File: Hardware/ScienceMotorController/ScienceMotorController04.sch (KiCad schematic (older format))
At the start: 4 parts

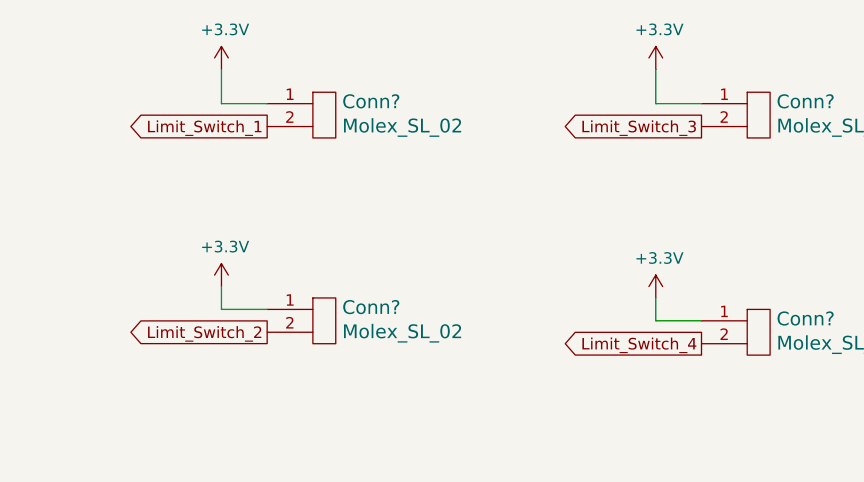
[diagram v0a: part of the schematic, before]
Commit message: limit switch indicators
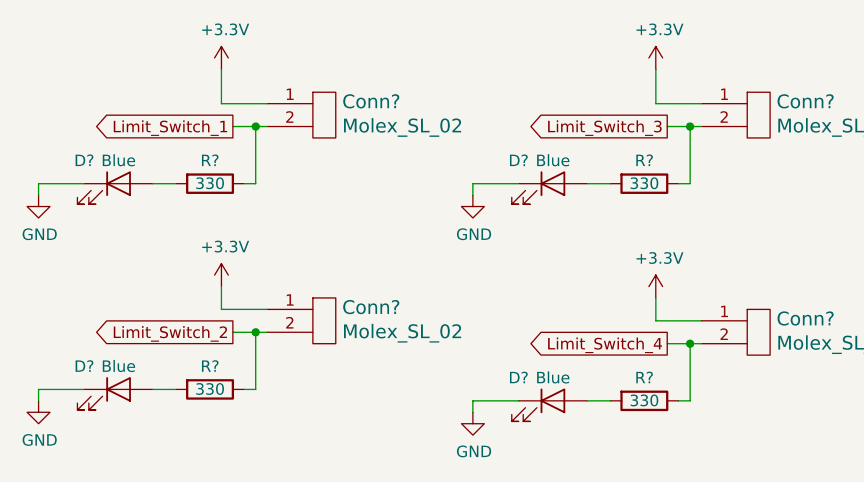
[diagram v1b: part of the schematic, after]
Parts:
- added D? (x4): Blue, symbol Device:LED
- added R? (x4): 330, symbol Device:R
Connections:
- net Limit_Switch_1: now also R?.1
- net Limit_Switch_2: now also R?.1
- net Limit_Switch_3: now also R?.1
- net Limit_Switch_4: now also R?.1
- new net: D?.2 (A), R?.2 (x4)
- new net GND: D?.1 (K), D?.1 (K), D?.1 (K), D?.1 (K)
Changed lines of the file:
@@
 $Descr A4 11693 8268
 encoding utf-8
-Sheet 5 11
+Sheet 11 11
 Title ""
 Date ""
@@
 Wire Wire Line
 	4150 2950 4350 2950
-Text GLabel 2450 2100 0    50   Output ~ 0
+Text GLabel 2300 2100 0    50   Output ~ 0
 Limit_Switch_1
-Text GLabel 2450 3000 0    50   Output ~ 0
+Text GLabel 2300 3000 0    50   Output ~ 0
 Limit_Switch_2
-Text GLabel 4350 2100 0    50   Output ~ 0
+Text GLabel 4200 2100 0    50   Output ~ 0
 Limit_Switch_3
-Text GLabel 4350 3050 0    50   Output ~ 0
+Text GLabel 4200 3050 0    50   Output ~ 0
 Limit_Switch_4
+Wire Wire Line
+	4350 2100 4300 2100
+Wire Wire Line
+	2450 2100 2400 2100
+Wire Wire Line
+	2450 3000 2400 3000
+Wire Wire Line
+	4200 3050 4300 3050
+$Comp
+L Device:LED D?
+U 1 1 5FAEAF9B
+P 3700 2350
+F 0 "D?" H 3550 2450 50  0000 C CNN
+F 1 "Blue" H 3700 2450 50  0000 C CNN
+F 2 "" H 3700 2350 50  0001 C CNN
+F 3 "~" H 3700 2350 50  0001 C CNN
+	1    3700 2350
+	1    0    0    -1
+$EndComp
+$Comp
+L Device:LED D?
+U 1 1 5FAEC8F1
+P 1800 2350
+F 0 "D?" H 1650 2450 50  0000 C CNN
+F 1 "Blue" H 1800 2450 50  0000 C CNN
+F 2 "" H 1800 2350 50  0001 C CNN
+F 3 "~" H 1800 2350 50  0001 C CNN
+	1    1800 2350
+	1    0    0    -1
+$EndComp
+$Comp
+L Device:LED D?
+U 1 1 5FAEE0DE
+P 1800 3250
+F 0 "D?" H 1650 3350 50  0000 C CNN
+F 1 "Blue" H 1800 3350 50  0000 C CNN
+F 2 "" H 1800 3250 50  0001 C CNN
+F 3 "~" H 1800 3250 50  0001 C CNN
+	1    1800 3250
+	1    0    0    -1
+$EndComp
+$Comp
+L Device:LED D?
+U 1 1 5FAEEC9D
+P 3700 3300
+F 0 "D?" H 3550 3400 50  0000 C CNN
+F 1 "Blue" H 3700 3400 50  0000 C CNN
+F 2 "" H 3700 3300 50  0001 C CNN
+F 3 "~" H 3700 3300 50  0001 C CNN
+	1    3700 3300
+	1    0    0    -1
+$EndComp
+$Comp
+L Device:R R?
+U 1 1 5FAEFC97
+P 4100 2350
+F 0 "R?" V 4000 2350 50  0000 C CNN
+F 1 "330" V 4100 2350 50  0000 C CNN
+F 2 "" V 4030 2350 50  0001 C CNN
+F 3 "~" H 4100 2350 50  0001 C CNN
+	1    4100 2350
+	0    1    1    0
+$EndComp
+Wire Wire Line
+	4250 2350 4300 2350
+Wire Wire Line
+	4300 2350 4300 2100
+Connection ~ 4300 2100
+Wire Wire Line
+	4300 2100 4200 2100
+Wire Wire Line
+	3950 2350 3850 2350
+$Comp
+L Device:R R?
+U 1 1 5FAF1AC8
+P 2200 2350
+F 0 "R?" V 2100 2350 50  0000 C CNN
+F 1 "330" V 2200 2350 50  0000 C CNN
+F 2 "" V 2130 2350 50  0001 C CNN
+F 3 "~" H 2200 2350 50  0001 C CNN
+	1    2200 2350
+	0    1    1    0
+$EndComp
+Wire Wire Line
+	2400 2100 2400 2350
+Wire Wire Line
+	2400 2350 2350 2350
+Connection ~ 2400 2100
+Wire Wire Line
+	2400 2100 2300 2100
+Wire Wire Line
+	1950 2350 2050 2350
+$Comp
+L Device:R R?
+U 1 1 5FAF47E1
+P 4100 3300
+F 0 "R?" V 4000 3300 50  0000 C CNN
+F 1 "330" V 4100 3300 50  0000 C CNN
+F 2 "" V 4030 3300 50  0001 C CNN
+F 3 "~" H 4100 3300 50  0001 C CNN
+	1    4100 3300
+	0    1    1    0
+$EndComp
+Wire Wire Line
+	3850 3300 3950 3300
+Wire Wire Line
+	4250 3300 4300 3300
+Wire Wire Line
+	4300 3300 4300 3050
+Connection ~ 4300 3050
+Wire Wire Line
+	4300 3050 4350 3050
+$Comp
+L Device:R R?
+U 1 1 5FAF884A
+P 2200 3250
+F 0 "R?" V 2100 3250 50  0000 C CNN
+F 1 "330" V 2200 3250 50  0000 C CNN
+F 2 "" V 2130 3250 50  0001 C CNN
+F 3 "~" H 2200 3250 50  0001 C CNN
+	1    2200 3250
+	0    1    1    0
+$EndComp
+Wire Wire Line
+	1950 3250 2050 3250
+Wire Wire Line
+	2350 3250 2400 3250
+Wire Wire Line
+	2400 3250 2400 3000
+Connection ~ 2400 3000
+Wire Wire Line
+	2400 3000 2300 3000
+$Comp
+L power:GND #PWR?
+U 1 1 5FAFA721
+P 3350 2400
+F 0 "#PWR?" H 3350 2150 50  0001 C CNN
+F 1 "GND" H 3355 2227 50  0000 C CNN
+F 2 "" H 3350 2400 50  0001 C CNN
+F 3 "" H 3350 2400 50  0001 C CNN
+	1    3350 2400
+	1    0    0    -1
+$EndComp
+$Comp
+L power:GND #PWR?
+U 1 1 5FAFC4B8
+P 1450 2400
+F 0 "#PWR?" H 1450 2150 50  0001 C CNN
+F 1 "GND" H 1455 2227 50  0000 C CNN
+F 2 "" H 1450 2400 50  0001 C CNN
+F 3 "" H 1450 2400 50  0001 C CNN
+	1    1450 2400
+	1    0    0    -1
+$EndComp
+$Comp
+L power:GND #PWR?
+U 1 1 5FAFD70B
+P 1450 3300
+F 0 "#PWR?" H 1450 3050 50  0001 C CNN
+F 1 "GND" H 1455 3127 50  0000 C CNN
+F 2 "" H 1450 3300 50  0001 C CNN
+F 3 "" H 1450 3300 50  0001 C CNN
+	1    1450 3300
+	1    0    0    -1
+$EndComp
+$Comp
+L power:GND #PWR?
+U 1 1 5FAFEF1A
+P 3350 3350
+F 0 "#PWR?" H 3350 3100 50  0001 C CNN
+F 1 "GND" H 3355 3177 50  0000 C CNN
+F 2 "" H 3350 3350 50  0001 C CNN
+F 3 "" H 3350 3350 50  0001 C CNN
+	1    3350 3350
+	1    0    0    -1
+$EndComp
+Wire Wire Line
+	3550 2350 3350 2350
+Wire Wire Line
+	3350 2350 3350 2400
+Wire Wire Line
+	3350 3350 3350 3300
+Wire Wire Line
+	3350 3300 3550 3300
+Wire Wire Line
+	1650 2350 1450 2350
+Wire Wire Line
+	1450 2350 1450 2400
+Wire Wire Line
+	1450 3300 1450 3250
+Wire Wire Line
+	1450 3250 1650 3250
 $EndSCHEMATC

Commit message: made some more hierarchal changes
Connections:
- net +3V3 renamed 3.3VA
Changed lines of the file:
@@
 $Descr A4 11693 8268
 encoding utf-8
-Sheet 11 10
+Sheet 4 10
 Title ""
 Date ""
@@
 	1    0    0    -1
 $EndComp
-$Comp
-L power:+3.3V #PWR?
-U 1 1 5F81D779
-P 2250 1850
-F 0 "#PWR?" H 2250 1700 50  0001 C CNN
-F 1 "+3.3V" H 2265 2023 50  0000 C CNN
-F 2 "" H 2250 1850 50  0001 C CNN
-F 3 "" H 2250 1850 50  0001 C CNN
-	1    2250 1850
-	1    0    0    -1
-$EndComp
-$Comp
-L power:+3.3V #PWR?
-U 1 1 5F81DF85
-P 4150 1850
-F 0 "#PWR?" H 4150 1700 50  0001 C CNN
-F 1 "+3.3V" H 4165 2023 50  0000 C CNN
-F 2 "" H 4150 1850 50  0001 C CNN
-F 3 "" H 4150 1850 50  0001 C CNN
-	1    4150 1850
-	1    0    0    -1
-$EndComp
-$Comp
-L power:+3.3V #PWR?
-U 1 1 5F81E7D7
-P 2250 2800
-F 0 "#PWR?" H 2250 2650 50  0001 C CNN
-F 1 "+3.3V" H 2265 2973 50  0000 C CNN
-F 2 "" H 2250 2800 50  0001 C CNN
-F 3 "" H 2250 2800 50  0001 C CNN
-	1    2250 2800
-	1    0    0    -1
-$EndComp
-$Comp
-L power:+3.3V #PWR?
-U 1 1 5F81F2A0
-P 4150 2850
-F 0 "#PWR?" H 4150 2700 50  0001 C CNN
-F 1 "+3.3V" H 4165 3023 50  0000 C CNN
-F 2 "" H 4150 2850 50  0001 C CNN
-F 3 "" H 4150 2850 50  0001 C CNN
-	1    4150 2850
-	1    0    0    -1
-$EndComp
 Wire Wire Line
 	2250 1850 2250 2000
@@
 Wire Wire Line
 	1450 3250 1650 3250
+Text HLabel 2250 1850 1    50   Input ~ 0
+3.3VA
+Text HLabel 4150 1850 1    50   Input ~ 0
+3.3VA
+Text HLabel 2250 2800 1    50   Input ~ 0
+3.3VA
+Text HLabel 4150 2850 1    50   Input ~ 0
+3.3VA
 $EndSCHEMATC

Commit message: fixed hierarchical
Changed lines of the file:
@@
 $Descr A4 11693 8268
 encoding utf-8
-Sheet 4 10
+Sheet 9 11
 Title ""
 Date ""
@@
 U 1 1 5F81B312
 P 2650 2150
+AR Path="/5F81B171/5F81B312" Ref="Conn?"  Part="1"
+AR Path="/5F7148FA/5FC42AEE/5F81B312" Ref="Conn?"  Part="1"
 F 0 "Conn?" H 2778 2308 60  0000 L CNN
 F 1 "Molex_SL_02" H 2778 2202 60  0000 L CNN
@@
 U 1 1 5F81C1D4
 P 4550 2150
+AR Path="/5F81B171/5F81C1D4" Ref="Conn?"  Part="1"
+AR Path="/5F7148FA/5FC42AEE/5F81C1D4" Ref="Conn?"  Part="1"
 F 0 "Conn?" H 4678 2308 60  0000 L CNN
 F 1 "Molex_SL_02" H 4678 2202 60  0000 L CNN
@@
 U 1 1 5F81C7E8
 P 2650 3050
+AR Path="/5F81B171/5F81C7E8" Ref="Conn?"  Part="1"
+AR Path="/5F7148FA/5FC42AEE/5F81C7E8" Ref="Conn?"  Part="1"
 F 0 "Conn?" H 2778 3208 60  0000 L CNN
 F 1 "Molex_SL_02" H 2778 3102 60  0000 L CNN
@@
 U 1 1 5F81D13D
 P 4550 3100
+AR Path="/5F81B171/5F81D13D" Ref="Conn?"  Part="1"
+AR Path="/5F7148FA/5FC42AEE/5F81D13D" Ref="Conn?"  Part="1"
 F 0 "Conn?" H 4678 3258 60  0000 L CNN
 F 1 "Molex_SL_02" H 4678 3152 60  0000 L CNN
@@
 Wire Wire Line
 	4150 2950 4350 2950
-Text GLabel 2300 2100 0    50   Output ~ 0
-Limit_Switch_1
-Text GLabel 2300 3000 0    50   Output ~ 0
-Limit_Switch_2
-Text GLabel 4200 2100 0    50   Output ~ 0
-Limit_Switch_3
-Text GLabel 4200 3050 0    50   Output ~ 0
-Limit_Switch_4
 Wire Wire Line
 	4350 2100 4300 2100
@@
 U 1 1 5FAEAF9B
 P 3700 2350
+AR Path="/5F81B171/5FAEAF9B" Ref="D?"  Part="1"
+AR Path="/5F7148FA/5FC42AEE/5FAEAF9B" Ref="D?"  Part="1"
 F 0 "D?" H 3550 2450 50  0000 C CNN
 F 1 "Blue" H 3700 2450 50  0000 C CNN
@@
 U 1 1 5FAEC8F1
 P 1800 2350
+AR Path="/5F81B171/5FAEC8F1" Ref="D?"  Part="1"
+AR Path="/5F7148FA/5FC42AEE/5FAEC8F1" Ref="D?"  Part="1"
 F 0 "D?" H 1650 2450 50  0000 C CNN
 F 1 "Blue" H 1800 2450 50  0000 C CNN
@@
 U 1 1 5FAEE0DE
 P 1800 3250
+AR Path="/5F81B171/5FAEE0DE" Ref="D?"  Part="1"
+AR Path="/5F7148FA/5FC42AEE/5FAEE0DE" Ref="D?"  Part="1"
 F 0 "D?" H 1650 3350 50  0000 C CNN
 F 1 "Blue" H 1800 3350 50  0000 C CNN
@@
 U 1 1 5FAEEC9D
 P 3700 3300
+AR Path="/5F81B171/5FAEEC9D" Ref="D?"  Part="1"
+AR Path="/5F7148FA/5FC42AEE/5FAEEC9D" Ref="D?"  Part="1"
 F 0 "D?" H 3550 3400 50  0000 C CNN
 F 1 "Blue" H 3700 3400 50  0000 C CNN
@@
 U 1 1 5FAEFC97
 P 4100 2350
+AR Path="/5F81B171/5FAEFC97" Ref="R?"  Part="1"
+AR Path="/5F7148FA/5FC42AEE/5FAEFC97" Ref="R?"  Part="1"
 F 0 "R?" V 4000 2350 50  0000 C CNN
 F 1 "330" V 4100 2350 50  0000 C CNN
@@
 U 1 1 5FAF1AC8
 P 2200 2350
+AR Path="/5F81B171/5FAF1AC8" Ref="R?"  Part="1"
+AR Path="/5F7148FA/5FC42AEE/5FAF1AC8" Ref="R?"  Part="1"
 F 0 "R?" V 2100 2350 50  0000 C CNN
 F 1 "330" V 2200 2350 50  0000 C CNN
@@
 U 1 1 5FAF47E1
 P 4100 3300
+AR Path="/5F81B171/5FAF47E1" Ref="R?"  Part="1"
+AR Path="/5F7148FA/5FC42AEE/5FAF47E1" Ref="R?"  Part="1"
 F 0 "R?" V 4000 3300 50  0000 C CNN
 F 1 "330" V 4100 3300 50  0000 C CNN
@@
 U 1 1 5FAF884A
 P 2200 3250
+AR Path="/5F81B171/5FAF884A" Ref="R?"  Part="1"
+AR Path="/5F7148FA/5FC42AEE/5FAF884A" Ref="R?"  Part="1"
 F 0 "R?" V 2100 3250 50  0000 C CNN
 F 1 "330" V 2200 3250 50  0000 C CNN
@@
 U 1 1 5FAFA721
 P 3350 2400
+AR Path="/5F81B171/5FAFA721" Ref="#PWR?"  Part="1"
+AR Path="/5F7148FA/5FC42AEE/5FAFA721" Ref="#PWR?"  Part="1"
 F 0 "#PWR?" H 3350 2150 50  0001 C CNN
 F 1 "GND" H 3355 2227 50  0000 C CNN
@@
 U 1 1 5FAFC4B8
 P 1450 2400
+AR Path="/5F81B171/5FAFC4B8" Ref="#PWR?"  Part="1"
+AR Path="/5F7148FA/5FC42AEE/5FAFC4B8" Ref="#PWR?"  Part="1"
 F 0 "#PWR?" H 1450 2150 50  0001 C CNN
 F 1 "GND" H 1455 2227 50  0000 C CNN
@@
 U 1 1 5FAFD70B
 P 1450 3300
+AR Path="/5F81B171/5FAFD70B" Ref="#PWR?"  Part="1"
+AR Path="/5F7148FA/5FC42AEE/5FAFD70B" Ref="#PWR?"  Part="1"
 F 0 "#PWR?" H 1450 3050 50  0001 C CNN
 F 1 "GND" H 1455 3127 50  0000 C CNN
@@
 U 1 1 5FAFEF1A
 P 3350 3350
+AR Path="/5F81B171/5FAFEF1A" Ref="#PWR?"  Part="1"
+AR Path="/5F7148FA/5FC42AEE/5FAFEF1A" Ref="#PWR?"  Part="1"
 F 0 "#PWR?" H 3350 3100 50  0001 C CNN
 F 1 "GND" H 3355 3177 50  0000 C CNN
@@
 Text HLabel 4150 2850 1    50   Input ~ 0
 3.3VA
+Text HLabel 2300 2100 0    50   Output ~ 0
+Limit_Switch_1
+Text HLabel 2300 3000 0    50   Output ~ 0
+Limit_Switch_2
+Text HLabel 4200 2100 0    50   Output ~ 0
+Limit_Switch_3
+Text HLabel 4200 3050 0    50   Output ~ 0
+Limit_Switch_4
 $EndSCHEMATC

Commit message: cleaned up sheet names
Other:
- note added: "Limit Switches"
- moved on the sheet: Conn?, D?, R?

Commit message: added logic line
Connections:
- net 3.3VA renamed 3.3V
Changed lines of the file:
@@
 	6850 5600 7050 5600
 Text HLabel 7650 4200 1    50   Input ~ 0
-3.3VA
+3.3V
 Text HLabel 9550 4200 1    50   Input ~ 0
-3.3VA
+3.3V
 Text HLabel 7650 5150 1    50   Input ~ 0
-3.3VA
+3.3V
 Text HLabel 9550 5200 1    50   Input ~ 0
-3.3VA
+3.3V
 Text HLabel 7700 4450 0    50   Output ~ 0
 Limit_Switch_1

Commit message: annotated
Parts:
- gave numbers to parts that had none: 12
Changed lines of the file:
@@
 P 8050 4500
 AR Path="/5F81B171/5F81B312" Ref="Conn?"  Part="1"
-AR Path="/5F7148FA/5FC42AEE/5F81B312" Ref="Conn?"  Part="1"
-F 0 "Conn?" H 8178 4658 60  0000 L CNN
+AR Path="/5F7148FA/5FC42AEE/5F81B312" Ref="Conn7"  Part="1"
+F 0 "Conn7" H 8178 4658 60  0000 L CNN
 F 1 "Molex_SL_02" H 8178 4552 60  0000 L CNN
 F 2 "" H 8050 4400 60  0001 C CNN
@@
 P 9950 4500
 AR Path="/5F81B171/5F81C1D4" Ref="Conn?"  Part="1"
-AR Path="/5F7148FA/5FC42AEE/5F81C1D4" Ref="Conn?"  Part="1"
-F 0 "Conn?" H 10078 4658 60  0000 L CNN
+AR Path="/5F7148FA/5FC42AEE/5F81C1D4" Ref="Conn9"  Part="1"
+F 0 "Conn9" H 10078 4658 60  0000 L CNN
 F 1 "Molex_SL_02" H 10078 4552 60  0000 L CNN
 F 2 "" H 9950 4400 60  0001 C CNN
@@
 P 8050 5400
 AR Path="/5F81B171/5F81C7E8" Ref="Conn?"  Part="1"
-AR Path="/5F7148FA/5FC42AEE/5F81C7E8" Ref="Conn?"  Part="1"
-F 0 "Conn?" H 8178 5558 60  0000 L CNN
+AR Path="/5F7148FA/5FC42AEE/5F81C7E8" Ref="Conn8"  Part="1"
+F 0 "Conn8" H 8178 5558 60  0000 L CNN
 F 1 "Molex_SL_02" H 8178 5452 60  0000 L CNN
 F 2 "" H 8050 5300 60  0001 C CNN
@@
 P 9950 5450
 AR Path="/5F81B171/5F81D13D" Ref="Conn?"  Part="1"
-AR Path="/5F7148FA/5FC42AEE/5F81D13D" Ref="Conn?"  Part="1"
-F 0 "Conn?" H 10078 5608 60  0000 L CNN
+AR Path="/5F7148FA/5FC42AEE/5F81D13D" Ref="Conn10"  Part="1"
+F 0 "Conn10" H 10078 5608 60  0000 L CNN
 F 1 "Molex_SL_02" H 10078 5502 60  0000 L CNN
 F 2 "" H 9950 5350 60  0001 C CNN
@@
 P 9100 4700
 AR Path="/5F81B171/5FAEAF9B" Ref="D?"  Part="1"
-AR Path="/5F7148FA/5FC42AEE/5FAEAF9B" Ref="D?"  Part="1"
-F 0 "D?" H 8950 4800 50  0000 C CNN
+AR Path="/5F7148FA/5FC42AEE/5FAEAF9B" Ref="D24"  Part="1"
+F 0 "D24" H 8950 4800 50  0000 C CNN
 F 1 "Blue" H 9100 4800 50  0000 C CNN
 F 2 "" H 9100 4700 50  0001 C CNN
@@
 P 7200 4700
 AR Path="/5F81B171/5FAEC8F1" Ref="D?"  Part="1"
-AR Path="/5F7148FA/5FC42AEE/5FAEC8F1" Ref="D?"  Part="1"
-F 0 "D?" H 7050 4800 50  0000 C CNN
+AR Path="/5F7148FA/5FC42AEE/5FAEC8F1" Ref="D22"  Part="1"
+F 0 "D22" H 7050 4800 50  0000 C CNN
 F 1 "Blue" H 7200 4800 50  0000 C CNN
 F 2 "" H 7200 4700 50  0001 C CNN
@@
 P 7200 5600
 AR Path="/5F81B171/5FAEE0DE" Ref="D?"  Part="1"
-AR Path="/5F7148FA/5FC42AEE/5FAEE0DE" Ref="D?"  Part="1"
-F 0 "D?" H 7050 5700 50  0000 C CNN
+AR Path="/5F7148FA/5FC42AEE/5FAEE0DE" Ref="D23"  Part="1"
+F 0 "D23" H 7050 5700 50  0000 C CNN
 F 1 "Blue" H 7200 5700 50  0000 C CNN
 F 2 "" H 7200 5600 50  0001 C CNN
@@
 P 9100 5650
 AR Path="/5F81B171/5FAEEC9D" Ref="D?"  Part="1"
-AR Path="/5F7148FA/5FC42AEE/5FAEEC9D" Ref="D?"  Part="1"
-F 0 "D?" H 8950 5750 50  0000 C CNN
+AR Path="/5F7148FA/5FC42AEE/5FAEEC9D" Ref="D25"  Part="1"
+F 0 "D25" H 8950 5750 50  0000 C CNN
 F 1 "Blue" H 9100 5750 50  0000 C CNN
 F 2 "" H 9100 5650 50  0001 C CNN
@@
 P 9500 4700
 AR Path="/5F81B171/5FAEFC97" Ref="R?"  Part="1"
-AR Path="/5F7148FA/5FC42AEE/5FAEFC97" Ref="R?"  Part="1"
-F 0 "R?" V 9400 4700 50  0000 C CNN
+AR Path="/5F7148FA/5FC42AEE/5FAEFC97" Ref="R53"  Part="1"
+F 0 "R53" V 9400 4700 50  0000 C CNN
 F 1 "330" V 9500 4700 50  0000 C CNN
 F 2 "" V 9430 4700 50  0001 C CNN
@@
 P 7600 4700
 AR Path="/5F81B171/5FAF1AC8" Ref="R?"  Part="1"
-AR Path="/5F7148FA/5FC42AEE/5FAF1AC8" Ref="R?"  Part="1"
-F 0 "R?" V 7500 4700 50  0000 C CNN
+AR Path="/5F7148FA/5FC42AEE/5FAF1AC8" Ref="R51"  Part="1"
+F 0 "R51" V 7500 4700 50  0000 C CNN
 F 1 "330" V 7600 4700 50  0000 C CNN
 F 2 "" V 7530 4700 50  0001 C CNN
@@
 P 9500 5650
 AR Path="/5F81B171/5FAF47E1" Ref="R?"  Part="1"
-AR Path="/5F7148FA/5FC42AEE/5FAF47E1" Ref="R?"  Part="1"
-F 0 "R?" V 9400 5650 50  0000 C CNN
+AR Path="/5F7148FA/5FC42AEE/5FAF47E1" Ref="R54"  Part="1"
+F 0 "R54" V 9400 5650 50  0000 C CNN
 F 1 "330" V 9500 5650 50  0000 C CNN
 F 2 "" V 9430 5650 50  0001 C CNN
@@
 P 7600 5600
 AR Path="/5F81B171/5FAF884A" Ref="R?"  Part="1"
-AR Path="/5F7148FA/5FC42AEE/5FAF884A" Ref="R?"  Part="1"
-F 0 "R?" V 7500 5600 50  0000 C CNN
+AR Path="/5F7148FA/5FC42AEE/5FAF884A" Ref="R52"  Part="1"
+F 0 "R52" V 7500 5600 50  0000 C CNN
 F 1 "330" V 7600 5600 50  0000 C CNN
 F 2 "" V 7530 5600 50  0001 C CNN
@@
 P 8750 4750
 AR Path="/5F81B171/5FAFA721" Ref="#PWR?"  Part="1"
-AR Path="/5F7148FA/5FC42AEE/5FAFA721" Ref="#PWR?"  Part="1"
-F 0 "#PWR?" H 8750 4500 50  0001 C CNN
+AR Path="/5F7148FA/5FC42AEE/5FAFA721" Ref="#PWR043"  Part="1"
+F 0 "#PWR043" H 8750 4500 50  0001 C CNN
 F 1 "GND" H 8755 4577 50  0000 C CNN
 F 2 "" H 8750 4750 50  0001 C CNN
@@
 P 6850 4750
 AR Path="/5F81B171/5FAFC4B8" Ref="#PWR?"  Part="1"
-AR Path="/5F7148FA/5FC42AEE/5FAFC4B8" Ref="#PWR?"  Part="1"
-F 0 "#PWR?" H 6850 4500 50  0001 C CNN
+AR Path="/5F7148FA/5FC42AEE/5FAFC4B8" Ref="#PWR041"  Part="1"
+F 0 "#PWR041" H 6850 4500 50  0001 C CNN
 F 1 "GND" H 6855 4577 50  0000 C CNN
 F 2 "" H 6850 4750 50  0001 C CNN
@@
 P 6850 5650
 AR Path="/5F81B171/5FAFD70B" Ref="#PWR?"  Part="1"
-AR Path="/5F7148FA/5FC42AEE/5FAFD70B" Ref="#PWR?"  Part="1"
-F 0 "#PWR?" H 6850 5400 50  0001 C CNN
+AR Path="/5F7148FA/5FC42AEE/5FAFD70B" Ref="#PWR042"  Part="1"
+F 0 "#PWR042" H 6850 5400 50  0001 C CNN
 F 1 "GND" H 6855 5477 50  0000 C CNN
 F 2 "" H 6850 5650 50  0001 C CNN
@@
 P 8750 5700
 AR Path="/5F81B171/5FAFEF1A" Ref="#PWR?"  Part="1"
-AR Path="/5F7148FA/5FC42AEE/5FAFEF1A" Ref="#PWR?"  Part="1"
-F 0 "#PWR?" H 8750 5450 50  0001 C CNN
+AR Path="/5F7148FA/5FC42AEE/5FAFEF1A" Ref="#PWR044"  Part="1"
+F 0 "#PWR044" H 8750 5450 50  0001 C CNN
 F 1 "GND" H 8755 5527 50  0000 C CNN
 F 2 "" H 8750 5700 50  0001 C CNN
